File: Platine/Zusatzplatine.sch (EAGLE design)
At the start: 25 parts

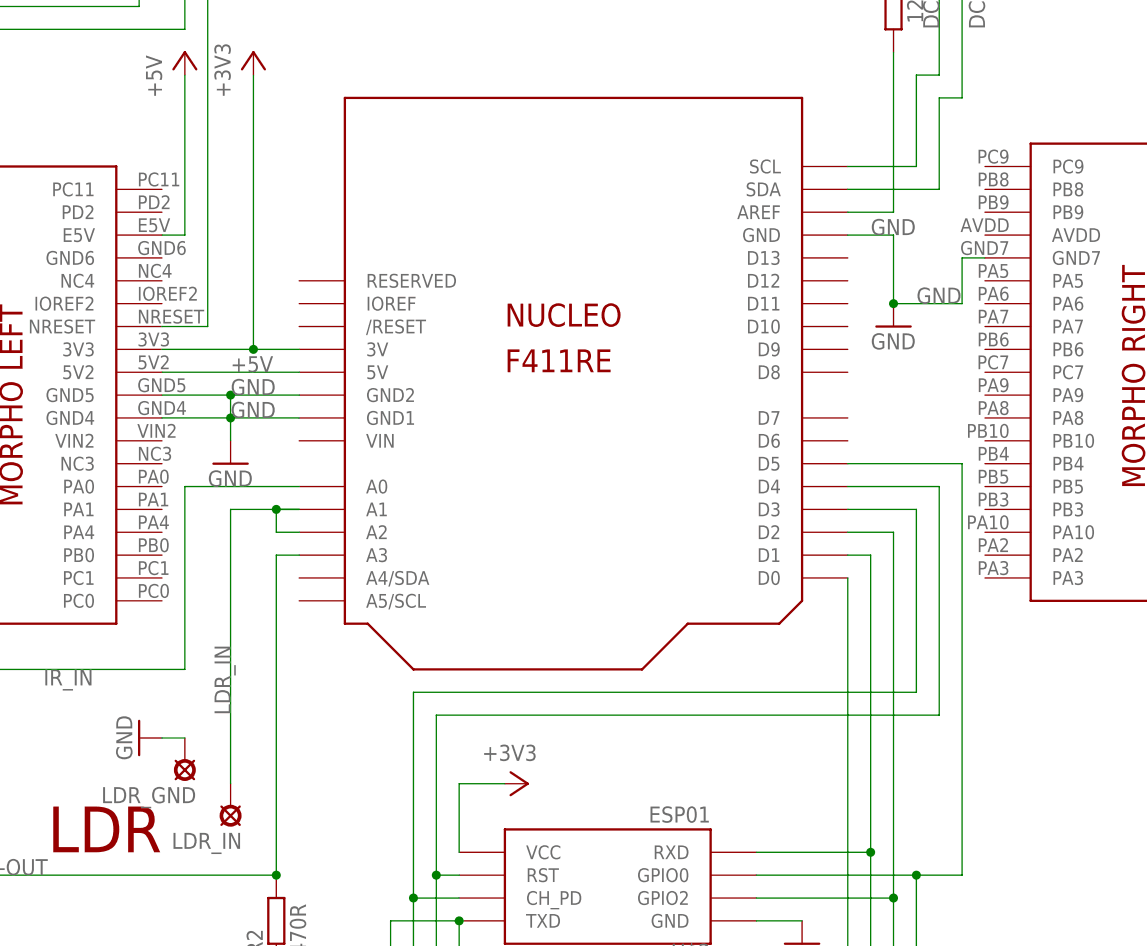
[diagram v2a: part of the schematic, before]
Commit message: - Parallele Verbindung zu Morpho-Connectors
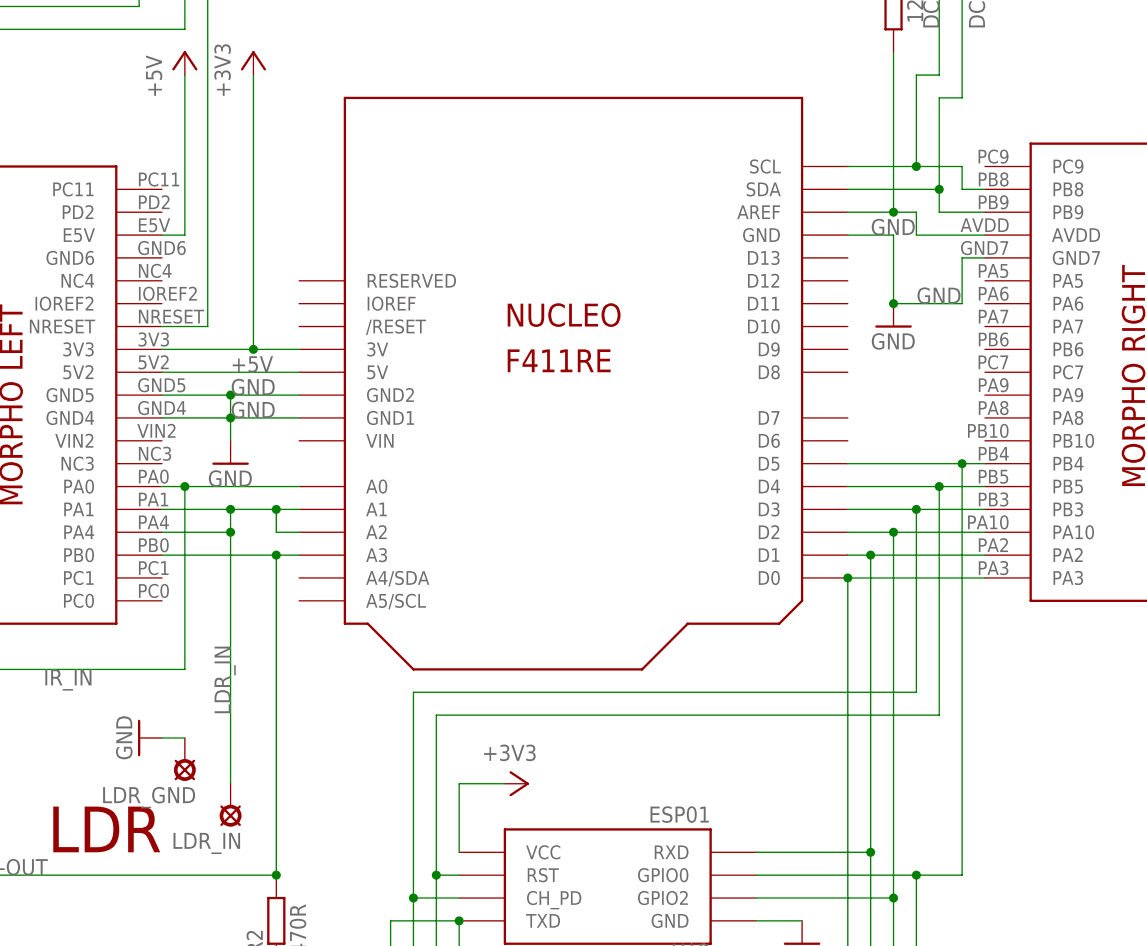
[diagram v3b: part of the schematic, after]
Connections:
- net DCF1_DATA: now also U$1.PB8
- net DCF1_PON: now also U$1.PB9
- net IR_IN: now also U$1.PA0
- net LDR_IN: now also U$1.PA1, U$1.PA4
- net LED-OUT: now also U$1.PB0
- net N$1: now also U$1.AVDD
- net N$12: now also U$1.PB4
- net N$13: now also U$1.PB5
- net N$14: now also U$1.PB3
- net N$15: now also U$1.PA3
- net N$16: now also U$1.PA2
- net N$17: now also U$1.PA10
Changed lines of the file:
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@@
 <wire x1="-76.2" y1="-167.64" x2="-76.2" y2="-160.02" width="0.1524" layer="91"/>
 <junction x="-2.54" y="-167.64"/>
+<pinref part="U$1" gate="G$1" pin="PB0"/>
+<wire x1="-2.54" y1="-132.08" x2="-15.24" y2="-132.08" width="0.1524" layer="91"/>
+<junction x="-2.54" y="-132.08"/>
 </segment>
 </net>
@@
 <wire x1="-2.54" y1="-129.54" x2="-2.54" y2="-127" width="0.1524" layer="91"/>
 <pinref part="U$1" gate="G$1" pin="A1"/>
-<wire x1="-2.54" y1="-127" x2="0" y2="-127" width="0.1524" layer="91"/>
 <wire x1="0" y1="-127" x2="-2.54" y2="-127" width="0.1524" layer="91"/>
 <wire x1="-2.54" y1="-127" x2="-7.62" y2="-127" width="0.1524" layer="91"/>
-<wire x1="-7.62" y1="-127" x2="-7.62" y2="-157.48" width="0.1524" layer="91"/>
+<wire x1="-7.62" y1="-127" x2="-7.62" y2="-129.54" width="0.1524" layer="91"/>
 <label x="-7.62" y="-149.86" size="1.778" layer="95" rot="R90"/>
 <junction x="-2.54" y="-127"/>
+<pinref part="U$1" gate="G$1" pin="PA1"/>
+<wire x1="-7.62" y1="-129.54" x2="-7.62" y2="-157.48" width="0.1524" layer="91"/>
+<wire x1="-7.62" y1="-127" x2="-15.24" y2="-127" width="0.1524" layer="91"/>
+<junction x="-7.62" y="-127"/>
+<pinref part="U$1" gate="G$1" pin="PA4"/>
+<wire x1="-15.24" y1="-129.54" x2="-7.62" y2="-129.54" width="0.1524" layer="91"/>
+<junction x="-7.62" y="-129.54"/>
 </segment>
 </net>
@@
 <wire x1="68.58" y1="-190.5" x2="68.58" y2="-167.64" width="0.1524" layer="91"/>
 <junction x="68.58" y="-167.64"/>
+<pinref part="U$1" gate="G$1" pin="PB4"/>
+<wire x1="73.66" y1="-121.92" x2="76.2" y2="-121.92" width="0.1524" layer="91"/>
+<junction x="73.66" y="-121.92"/>
 </segment>
 </net>
@@
 <wire x1="15.24" y1="-190.5" x2="17.78" y2="-190.5" width="0.1524" layer="91"/>
 <junction x="15.24" y="-167.64"/>
+<pinref part="U$1" gate="G$1" pin="PB5"/>
+<wire x1="71.12" y1="-124.46" x2="76.2" y2="-124.46" width="0.1524" layer="91"/>
+<junction x="71.12" y="-124.46"/>
 </segment>
 </net>
@@
 <wire x1="12.7" y1="-193.04" x2="17.78" y2="-193.04" width="0.1524" layer="91"/>
 <junction x="12.7" y="-170.18"/>
+<pinref part="U$1" gate="G$1" pin="PB3"/>
+<wire x1="68.58" y1="-127" x2="76.2" y2="-127" width="0.1524" layer="91"/>
+<junction x="68.58" y="-127"/>
 </segment>
 </net>
@@
 <wire x1="10.16" y1="-172.72" x2="17.78" y2="-172.72" width="0.1524" layer="91"/>
 <junction x="17.78" y="-172.72"/>
+<pinref part="U$1" gate="G$1" pin="PA3"/>
+<wire x1="60.96" y1="-134.62" x2="76.2" y2="-134.62" width="0.1524" layer="91"/>
+<junction x="60.96" y="-134.62"/>
 </segment>
 </net>
@@
 <wire x1="63.5" y1="-187.96" x2="63.5" y2="-165.1" width="0.1524" layer="91"/>
 <junction x="63.5" y="-165.1"/>
+<pinref part="U$1" gate="G$1" pin="PA2"/>
+<wire x1="63.5" y1="-132.08" x2="76.2" y2="-132.08" width="0.1524" layer="91"/>
+<junction x="63.5" y="-132.08"/>
 </segment>
 </net>
@@
 <wire x1="66.04" y1="-193.04" x2="66.04" y2="-170.18" width="0.1524" layer="91"/>
 <junction x="66.04" y="-170.18"/>
+<pinref part="U$1" gate="G$1" pin="PA10"/>
+<wire x1="66.04" y1="-129.54" x2="76.2" y2="-129.54" width="0.1524" layer="91"/>
+<junction x="66.04" y="-129.54"/>
 </segment>
 </net>
@@
 <pinref part="U$1" gate="G$1" pin="SDA"/>
 <wire x1="71.12" y1="-91.44" x2="60.96" y2="-91.44" width="0.1524" layer="91"/>
+<wire x1="71.12" y1="-91.44" x2="71.12" y2="-93.98" width="0.1524" layer="91"/>
+<junction x="71.12" y="-91.44"/>
+<pinref part="U$1" gate="G$1" pin="PB9"/>
+<wire x1="71.12" y1="-93.98" x2="76.2" y2="-93.98" width="0.1524" layer="91"/>
 </segment>
 </net>
@@
 <pinref part="U$1" gate="G$1" pin="SCL"/>
 <wire x1="68.58" y1="-88.9" x2="60.96" y2="-88.9" width="0.1524" layer="91"/>
+<pinref part="U$1" gate="G$1" pin="PB8"/>
+<wire x1="76.2" y1="-91.44" x2="73.66" y2="-91.44" width="0.1524" layer="91"/>
+<wire x1="73.66" y1="-91.44" x2="73.66" y2="-88.9" width="0.1524" layer="91"/>
+<wire x1="73.66" y1="-88.9" x2="68.58" y2="-88.9" width="0.1524" layer="91"/>
+<junction x="68.58" y="-88.9"/>
 </segment>
 </net>
@@
 <pinref part="R3" gate="G$1" pin="2"/>
 <wire x1="66.04" y1="-76.2" x2="66.04" y2="-93.98" width="0.1524" layer="91"/>
+<wire x1="66.04" y1="-93.98" x2="68.58" y2="-93.98" width="0.1524" layer="91"/>
+<junction x="66.04" y="-93.98"/>
+<wire x1="68.58" y1="-93.98" x2="68.58" y2="-96.52" width="0.1524" layer="91"/>
+<pinref part="U$1" gate="G$1" pin="AVDD"/>
+<wire x1="68.58" y1="-96.52" x2="76.2" y2="-96.52" width="0.1524" layer="91"/>
 </segment>
 </net>
@@
 <wire x1="-35.56" y1="-144.78" x2="-35.56" y2="-152.4" width="0.1524" layer="91"/>
 <label x="-22.86" y="-144.78" size="1.778" layer="95" rot="R180"/>
-</segment>
-</net>
+<pinref part="U$1" gate="G$1" pin="PA0"/>
+<wire x1="-12.7" y1="-124.46" x2="-15.24" y2="-124.46" width="0.1524" layer="91"/>
+<junction x="-12.7" y="-124.46"/>
+</segment>
+</net>
